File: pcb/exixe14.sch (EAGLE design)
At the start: 51 parts

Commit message: refining board design for production run
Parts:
- removed R17: 10K, joyAnalog:RESISTOR0805-RES
- renumbered U$2 to IC1
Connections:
- net +3V3: no longer R17.2
- net NRST: no longer R17.1
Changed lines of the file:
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@@
 <parts>
 <part name="N1" library="russian-nixies" deviceset="IN-14" device=""/>
-<part name="U$2" library="nixx" deviceset="STM32F042K6" device=""/>
+<part name="IC1" library="nixx" deviceset="STM32F042K6" device=""/>
 <part name="JP2" library="pinhead" deviceset="PINHD-1X7" device=""/>
 <part name="Q1" library="nixx" deviceset="BF820" device=""/>
@@
 <part name="R15" library="joyAnalog" deviceset="RESISTOR" device="0805-RES" value="680"/>
 <part name="R16" library="joyAnalog" deviceset="RESISTOR" device="0805-RES" value="330"/>
-<part name="R17" library="joyAnalog" deviceset="RESISTOR" device="0805-RES" value="10K"/>
 <part name="R18" library="joyAnalog" deviceset="RESISTOR" device="0805-RES" value="10K"/>
-<part name="+3V5" library="joyAnalog" deviceset="+3V3" device=""/>
 <part name="+3V6" library="joyAnalog" deviceset="+3V3" device=""/>
 <part name="TP1" library="testpad" deviceset="PTR1" device="TP13R" value="PTR1TP13R"/>
@@
 <instances>
 <instance part="N1" gate="G$1" x="220.98" y="-30.48"/>
-<instance part="U$2" gate="G$1" x="386.08" y="104.14"/>
+<instance part="IC1" gate="G$1" x="386.08" y="104.14"/>
 <instance part="JP2" gate="A" x="332.74" y="-40.64"/>
 <instance part="Q1" gate="A" x="101.6" y="48.26"/>
@@
 <instance part="R15" gate="G$1" x="495.3" y="7.62"/>
 <instance part="R16" gate="G$1" x="495.3" y="-7.62"/>
-<instance part="R17" gate="G$1" x="340.36" y="-27.94" rot="R90"/>
 <instance part="R18" gate="G$1" x="347.98" y="-38.1" rot="R90"/>
-<instance part="+3V5" gate="G$1" x="340.36" y="-20.32" rot="MR0"/>
 <instance part="+3V6" gate="G$1" x="347.98" y="-30.48" rot="MR0"/>
 <instance part="TP1" gate="G$1" x="381" y="55.88" rot="R270"/>
@@
 <segment>
 <pinref part="GND13" gate="1" pin="GND"/>
-<pinref part="U$2" gate="G$1" pin="VSS"/>
+<pinref part="IC1" gate="G$1" pin="VSS"/>
 <wire x1="375.92" y1="38.1" x2="383.54" y2="38.1" width="0.1524" layer="91"/>
 </segment>
@@
 <segment>
 <pinref part="+3V1" gate="G$1" pin="+3V3"/>
-<pinref part="U$2" gate="G$1" pin="VDD"/>
+<pinref part="IC1" gate="G$1" pin="VDD"/>
 <wire x1="375.92" y1="101.6" x2="383.54" y2="101.6" width="0.1524" layer="91"/>
-<pinref part="U$2" gate="G$1" pin="VDDA"/>
+<pinref part="IC1" gate="G$1" pin="VDDA"/>
 <wire x1="383.54" y1="99.06" x2="375.92" y2="99.06" width="0.1524" layer="91"/>
 <wire x1="375.92" y1="99.06" x2="375.92" y2="101.6" width="0.1524" layer="91"/>
@@
 <pinref part="D1" gate="G$1" pin="A"/>
 <wire x1="459.74" y1="0" x2="467.36" y2="0" width="0.1524" layer="91"/>
-</segment>
-<segment>
-<pinref part="R17" gate="G$1" pin="2"/>
-<pinref part="+3V5" gate="G$1" pin="+3V3"/>
 </segment>
 <segment>
@@
 </segment>
 <segment>
-<pinref part="U$2" gate="G$1" pin="PA5"/>
+<pinref part="IC1" gate="G$1" pin="PA5"/>
 <wire x1="439.42" y1="88.9" x2="424.18" y2="88.9" width="0.1524" layer="91"/>
 <label x="426.72" y="88.9" size="1.778" layer="95"/>
@@
 </segment>
 <segment>
-<pinref part="U$2" gate="G$1" pin="PA6"/>
+<pinref part="IC1" gate="G$1" pin="PA6"/>
 <wire x1="439.42" y1="86.36" x2="424.18" y2="86.36" width="0.1524" layer="91"/>
 <label x="426.72" y="86.36" size="1.778" layer="95"/>
@@
 </segment>
 <segment>
-<pinref part="U$2" gate="G$1" pin="PA7"/>
+<pinref part="IC1" gate="G$1" pin="PA7"/>
 <wire x1="439.42" y1="83.82" x2="424.18" y2="83.82" width="0.1524" layer="91"/>
 <label x="426.72" y="83.82" size="1.778" layer="95"/>
@@
 <segment>
 <label x="426.72" y="60.96" size="1.778" layer="95"/>
-<pinref part="U$2" gate="G$1" pin="PA15"/>
+<pinref part="IC1" gate="G$1" pin="PA15"/>
 <wire x1="439.42" y1="60.96" x2="424.18" y2="60.96" width="0.1524" layer="91"/>
 </segment>
@@
 </segment>
 <segment>
-<pinref part="U$2" gate="G$1" pin="PA13/SWDIO"/>
+<pinref part="IC1" gate="G$1" pin="PA13/SWDIO"/>
 <wire x1="439.42" y1="66.04" x2="424.18" y2="66.04" width="0.1524" layer="91"/>
 <label x="426.72" y="66.04" size="1.778" layer="95"/>
@@
 </segment>
 <segment>
-<pinref part="U$2" gate="G$1" pin="PA14/SWCLK"/>
+<pinref part="IC1" gate="G$1" pin="PA14/SWCLK"/>
 <wire x1="439.42" y1="63.5" x2="424.18" y2="63.5" width="0.1524" layer="91"/>
 <label x="426.72" y="63.5" size="1.778" layer="95"/>
@@
 <net name="NRST" class="0">
 <segment>
-<pinref part="U$2" gate="G$1" pin="NRST"/>
+<pinref part="IC1" gate="G$1" pin="NRST"/>
 <wire x1="370.84" y1="78.74" x2="383.54" y2="78.74" width="0.1524" layer="91"/>
 <label x="370.84" y="78.74" size="1.778" layer="95"/>
@@
 <wire x1="307.34" y1="-33.02" x2="330.2" y2="-33.02" width="0.1524" layer="91"/>
 <label x="307.34" y="-33.02" size="1.778" layer="95"/>
-<pinref part="R17" gate="G$1" pin="1"/>
-<wire x1="340.36" y1="-33.02" x2="330.2" y2="-33.02" width="0.1524" layer="91"/>
-<junction x="330.2" y="-33.02"/>
 </segment>
 </net>
 <net name="UART_TX" class="0">
 <segment>
-<pinref part="U$2" gate="G$1" pin="PB6"/>
+<pinref part="IC1" gate="G$1" pin="PB6"/>
 <wire x1="439.42" y1="43.18" x2="424.18" y2="43.18" width="0.1524" layer="91"/>
 <label x="426.72" y="43.18" size="1.778" layer="95"/>
@@
 <segment>
 <label x="426.72" y="48.26" size="1.778" layer="95"/>
-<pinref part="U$2" gate="G$1" pin="PB4"/>
+<pinref part="IC1" gate="G$1" pin="PB4"/>
 <wire x1="439.42" y1="48.26" x2="424.18" y2="48.26" width="0.1524" layer="91"/>
 </segment>
@@
 </segment>
 <segment>
-<pinref part="U$2" gate="G$1" pin="PB8"/>
+<pinref part="IC1" gate="G$1" pin="PB8"/>
 <label x="426.72" y="38.1" size="1.778" layer="95"/>
 <wire x1="439.42" y1="38.1" x2="429.26" y2="38.1" width="0.1524" layer="91"/>
@@
 </segment>
 <segment>
-<pinref part="U$2" gate="G$1" pin="PA10"/>
+<pinref part="IC1" gate="G$1" pin="PA10"/>
 <wire x1="439.42" y1="73.66" x2="424.18" y2="73.66" width="0.1524" layer="91"/>
 <label x="426.72" y="73.66" size="1.778" layer="95"/>
@@
 <segment>
 <label x="426.72" y="45.72" size="1.778" layer="95"/>
-<pinref part="U$2" gate="G$1" pin="PB5"/>
+<pinref part="IC1" gate="G$1" pin="PB5"/>
 <wire x1="439.42" y1="45.72" x2="424.18" y2="45.72" width="0.1524" layer="91"/>
 </segment>
@@
 </segment>
 <segment>
-<pinref part="U$2" gate="G$1" pin="PA8"/>
+<pinref part="IC1" gate="G$1" pin="PA8"/>
 <wire x1="439.42" y1="78.74" x2="424.18" y2="78.74" width="0.1524" layer="91"/>
 <label x="426.72" y="78.74" size="1.778" layer="95"/>
@@
 </segment>
 <segment>
-<pinref part="U$2" gate="G$1" pin="PA9"/>
+<pinref part="IC1" gate="G$1" pin="PA9"/>
 <wire x1="439.42" y1="76.2" x2="424.18" y2="76.2" width="0.1524" layer="91"/>
 <label x="426.72" y="76.2" size="1.778" layer="95"/>
@@
 </segment>
 <segment>
-<pinref part="U$2" gate="G$1" pin="PA11"/>
+<pinref part="IC1" gate="G$1" pin="PA11"/>
 <wire x1="439.42" y1="71.12" x2="424.18" y2="71.12" width="0.1524" layer="91"/>
 <label x="426.72" y="71.12" size="1.778" layer="95"/>
@@
 </segment>
 <segment>
-<pinref part="U$2" gate="G$1" pin="PA0"/>
+<pinref part="IC1" gate="G$1" pin="PA0"/>
 <wire x1="439.42" y1="101.6" x2="424.18" y2="101.6" width="0.1524" layer="91"/>
 <label x="426.72" y="101.6" size="1.778" layer="95"/>
@@
 <segment>
 <label x="426.72" y="40.64" size="1.778" layer="95"/>
-<pinref part="U$2" gate="G$1" pin="PB7"/>
+<pinref part="IC1" gate="G$1" pin="PB7"/>
 <wire x1="439.42" y1="40.64" x2="424.18" y2="40.64" width="0.1524" layer="91"/>
 </segment>
@@
 </segment>
 <segment>
-<pinref part="U$2" gate="G$1" pin="PA3"/>
+<pinref part="IC1" gate="G$1" pin="PA3"/>
 <wire x1="439.42" y1="93.98" x2="424.18" y2="93.98" width="0.1524" layer="91"/>
 <label x="426.72" y="93.98" size="1.778" layer="95"/>
@@
 </segment>
 <segment>
-<pinref part="U$2" gate="G$1" pin="PA2"/>
+<pinref part="IC1" gate="G$1" pin="PA2"/>
 <wire x1="439.42" y1="96.52" x2="424.18" y2="96.52" width="0.1524" layer="91"/>
 <label x="426.72" y="96.52" size="1.778" layer="95"/>
@@
 </segment>
 <segment>
-<pinref part="U$2" gate="G$1" pin="PA1"/>
+<pinref part="IC1" gate="G$1" pin="PA1"/>
 <wire x1="439.42" y1="99.06" x2="424.18" y2="99.06" width="0.1524" layer="91"/>
 <label x="426.72" y="99.06" size="1.778" layer="95"/>
@@
 <segment>
 <wire x1="439.42" y1="55.88" x2="424.18" y2="55.88" width="0.1524" layer="91"/>
-<pinref part="U$2" gate="G$1" pin="PB0"/>
+<pinref part="IC1" gate="G$1" pin="PB0"/>
 <label x="426.72" y="55.88" size="1.778" layer="95"/>
 </segment>
@@
 </segment>
 <segment>
-<pinref part="U$2" gate="G$1" pin="PA4"/>
+<pinref part="IC1" gate="G$1" pin="PA4"/>
 <wire x1="439.42" y1="91.44" x2="424.18" y2="91.44" width="0.1524" layer="91"/>
 <label x="426.72" y="91.44" size="1.778" layer="95"/>
@@
 </segment>
 <segment>
-<pinref part="U$2" gate="G$1" pin="PB1"/>
+<pinref part="IC1" gate="G$1" pin="PB1"/>
 <wire x1="439.42" y1="53.34" x2="424.18" y2="53.34" width="0.1524" layer="91"/>
 <label x="426.72" y="53.34" size="1.778" layer="95"/>
@@
 <net name="N$2" class="0">
 <segment>
-<pinref part="U$2" gate="G$1" pin="PF0/OSC_IN"/>
+<pinref part="IC1" gate="G$1" pin="PF0/OSC_IN"/>
 <pinref part="TP1" gate="G$1" pin="TP"/>
 </segment>
@@
 <net name="N$16" class="0">
 <segment>
-<pinref part="U$2" gate="G$1" pin="PF1/OSC_OUT"/>
+<pinref part="IC1" gate="G$1" pin="PF1/OSC_OUT"/>
 <pinref part="TP2" gate="G$1" pin="TP"/>
 </segment>
@@
 <net name="BAKE" class="0">
 <segment>
-<pinref part="U$2" gate="G$1" pin="PA12"/>
+<pinref part="IC1" gate="G$1" pin="PA12"/>
 <wire x1="439.42" y1="68.58" x2="424.18" y2="68.58" width="0.1524" layer="91"/>
 <label x="426.72" y="68.58" size="1.778" layer="95"/>
@@
 <net name="N$25" class="0">
 <segment>
-<pinref part="U$2" gate="G$1" pin="PB3"/>
+<pinref part="IC1" gate="G$1" pin="PB3"/>
 <pinref part="TP4" gate="G$1" pin="TP"/>
 <wire x1="424.18" y1="50.8" x2="449.58" y2="50.8" width="0.1524" layer="91"/>

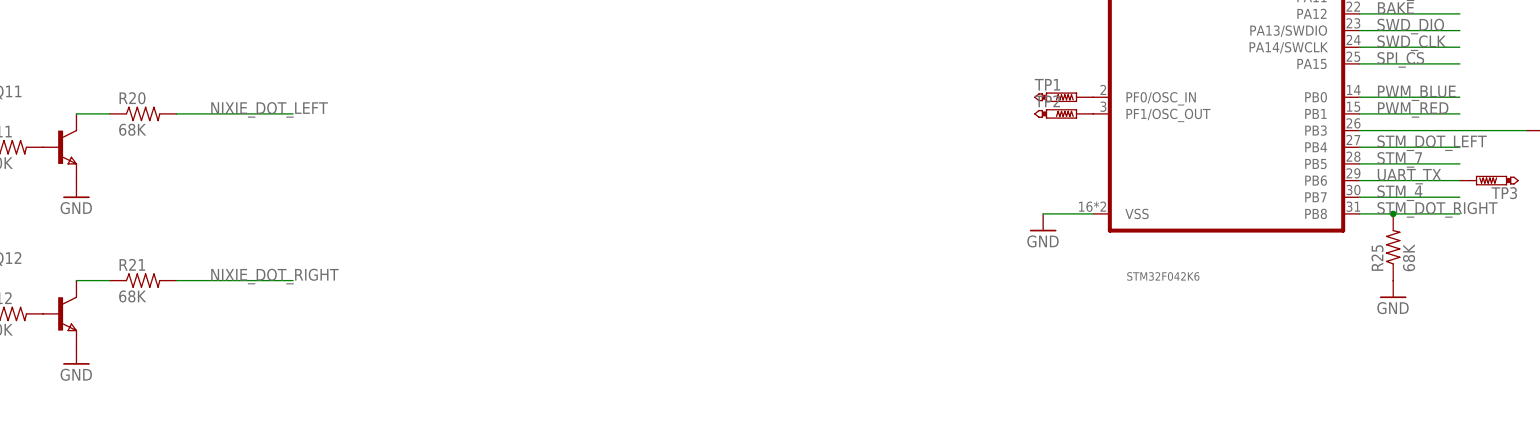
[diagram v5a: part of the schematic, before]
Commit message: adjusted passive values
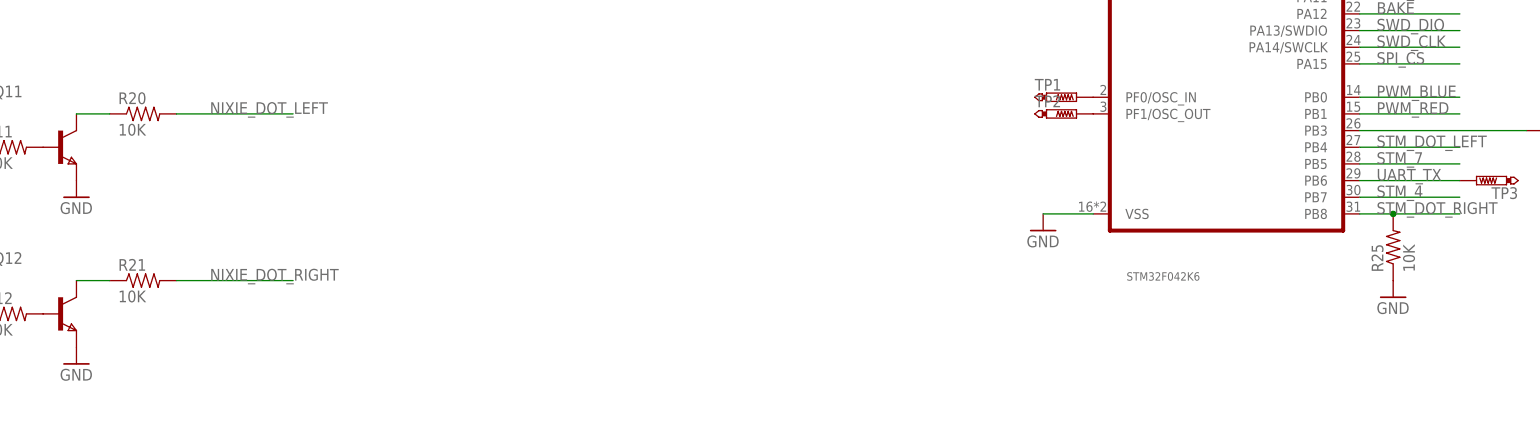
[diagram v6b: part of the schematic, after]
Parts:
- R20, R21, R25: value 68K -> 10K
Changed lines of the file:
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@@
 <part name="TP2" library="testpad" deviceset="PTR1" device="TP13R" value="PTR1TP13R"/>
 <part name="TP3" library="testpad" deviceset="PTR1" device="TP13R" value="PTR1TP13R"/>
-<part name="R20" library="joyAnalog" deviceset="RESISTOR" device="0805-RES" value="68K"/>
-<part name="R21" library="joyAnalog" deviceset="RESISTOR" device="0805-RES" value="68K"/>
-<part name="R25" library="joyAnalog" deviceset="RESISTOR" device="0805-RES" value="68K"/>
+<part name="R20" library="joyAnalog" deviceset="RESISTOR" device="0805-RES" value="10K"/>
+<part name="R21" library="joyAnalog" deviceset="RESISTOR" device="0805-RES" value="10K"/>
+<part name="R25" library="joyAnalog" deviceset="RESISTOR" device="0805-RES" value="10K"/>
 <part name="GND16" library="joyAnalog" deviceset="GND" device=""/>
 <part name="TP4" library="testpad" deviceset="PTR1" device="TP13R" value="PTR1TP13R"/>

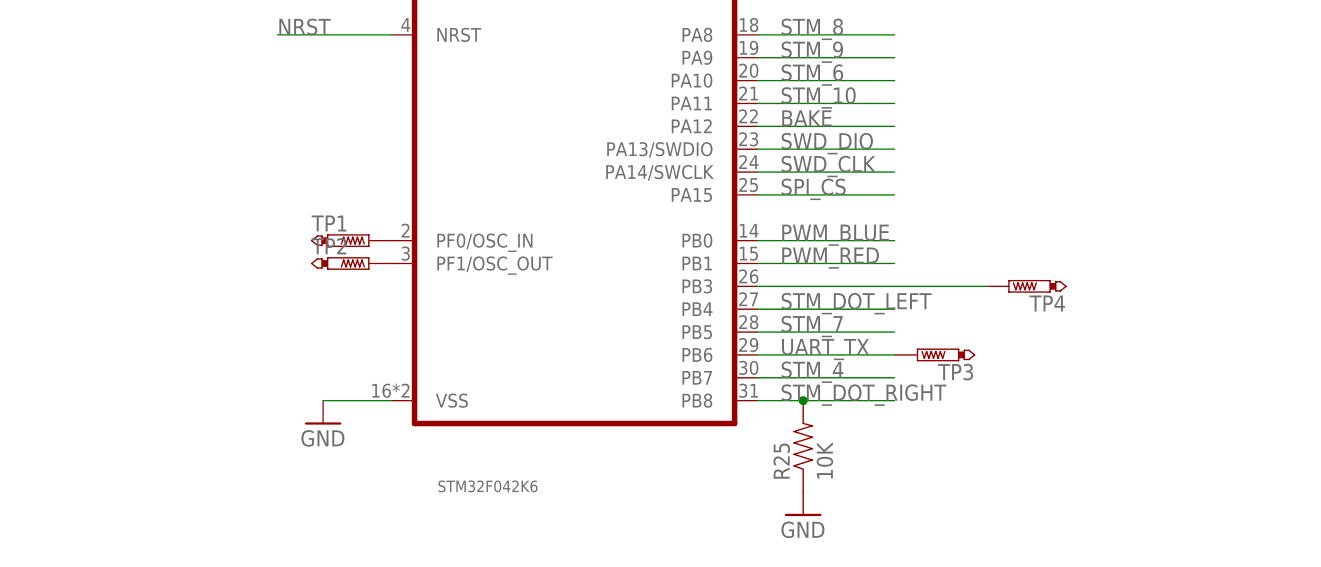
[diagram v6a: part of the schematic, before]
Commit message: changed testpoints to unpopulated resistors
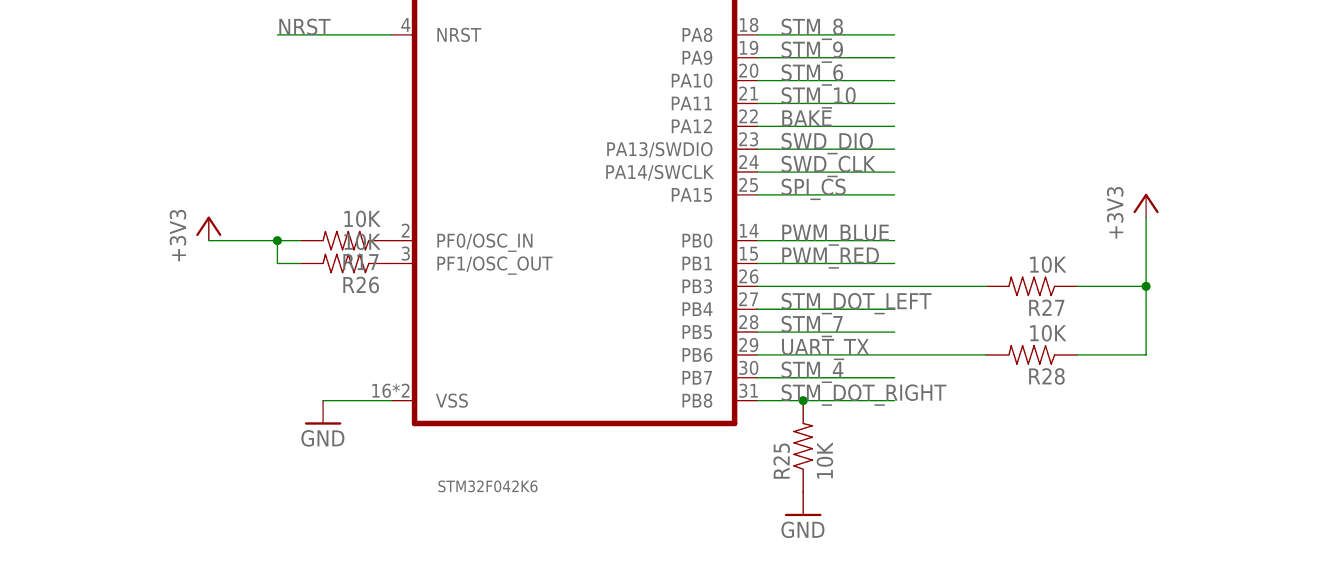
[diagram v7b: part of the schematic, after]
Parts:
- removed TP1, TP2, TP3, TP4: PTR1TP13R, testpad:PTR1TP13R
- added R17, R26, R27, R28: 10K, joyAnalog:RESISTOR0805-RES
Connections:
- net +3V3: now also R17.2, R26.2, R27.1, R28.1
- net N$16: now also R26.1; no longer TP2.TP
- net N$2: now also R17.1; no longer TP1.TP
- net N$25: now also R27.2; no longer TP4.TP
- net UART_TX: now also R28.2; no longer TP3.TP
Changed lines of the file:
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@@
 <part name="R18" library="joyAnalog" deviceset="RESISTOR" device="0805-RES" value="10K"/>
 <part name="+3V6" library="joyAnalog" deviceset="+3V3" device=""/>
-<part name="TP1" library="testpad" deviceset="PTR1" device="TP13R" value="PTR1TP13R"/>
 <part name="R22" library="joyAnalog" deviceset="RESISTOR" device="0805-RES" value="1M"/>
 <part name="R23" library="joyAnalog" deviceset="RESISTOR" device="0805-RES" value="68K"/>
@@
 <part name="GND18" library="joyAnalog" deviceset="GND" device=""/>
 <part name="R19" library="joyAnalog" deviceset="RESISTOR" device="0805-RES" value="1M"/>
-<part name="TP2" library="testpad" deviceset="PTR1" device="TP13R" value="PTR1TP13R"/>
-<part name="TP3" library="testpad" deviceset="PTR1" device="TP13R" value="PTR1TP13R"/>
 <part name="R20" library="joyAnalog" deviceset="RESISTOR" device="0805-RES" value="10K"/>
 <part name="R21" library="joyAnalog" deviceset="RESISTOR" device="0805-RES" value="10K"/>
 <part name="R25" library="joyAnalog" deviceset="RESISTOR" device="0805-RES" value="10K"/>
 <part name="GND16" library="joyAnalog" deviceset="GND" device=""/>
-<part name="TP4" library="testpad" deviceset="PTR1" device="TP13R" value="PTR1TP13R"/>
+<part name="+3V5" library="joyAnalog" deviceset="+3V3" device=""/>
+<part name="R17" library="joyAnalog" deviceset="RESISTOR" device="0805-RES" value="10K"/>
+<part name="R26" library="joyAnalog" deviceset="RESISTOR" device="0805-RES" value="10K"/>
+<part name="+3V7" library="joyAnalog" deviceset="+3V3" device=""/>
+<part name="R27" library="joyAnalog" deviceset="RESISTOR" device="0805-RES" value="10K"/>
+<part name="R28" library="joyAnalog" deviceset="RESISTOR" device="0805-RES" value="10K"/>
 </parts>
 <sheets>
@@
 <instance part="R18" gate="G$1" x="347.98" y="-38.1" rot="R90"/>
 <instance part="+3V6" gate="G$1" x="347.98" y="-30.48" rot="MR0"/>
-<instance part="TP1" gate="G$1" x="381" y="55.88" rot="R270"/>
 <instance part="R22" gate="G$1" x="391.16" y="-63.5" rot="R180"/>
 <instance part="R23" gate="G$1" x="406.4" y="-73.66" rot="R90"/>
@@
 <instance part="GND18" gate="1" x="378.46" y="-76.2"/>
 <instance part="R19" gate="G$1" x="378.46" y="-58.42" rot="R270"/>
-<instance part="TP2" gate="G$1" x="381" y="53.34" rot="R270"/>
-<instance part="TP3" gate="G$1" x="441.96" y="43.18" rot="R90"/>
 <instance part="R20" gate="G$1" x="238.76" y="53.34"/>
 <instance part="R21" gate="G$1" x="238.76" y="27.94"/>
 <instance part="R25" gate="G$1" x="429.26" y="33.02" rot="R90"/>
 <instance part="GND16" gate="1" x="429.26" y="25.4"/>
-<instance part="TP4" gate="G$1" x="452.12" y="50.8" rot="R90"/>
+<instance part="+3V5" gate="G$1" x="363.22" y="58.42"/>
+<instance part="R17" gate="G$1" x="378.46" y="55.88" rot="R180"/>
+<instance part="R26" gate="G$1" x="378.46" y="53.34" rot="R180"/>
+<instance part="+3V7" gate="G$1" x="467.36" y="60.96"/>
+<instance part="R27" gate="G$1" x="454.66" y="50.8" rot="R180"/>
+<instance part="R28" gate="G$1" x="454.66" y="43.18" rot="R180"/>
 </instances>
 <busses>
@@
 <wire x1="424.18" y1="-45.72" x2="431.8" y2="-45.72" width="0.1524" layer="91"/>
 </segment>
+<segment>
+<pinref part="+3V5" gate="G$1" pin="+3V3"/>
+<pinref part="R17" gate="G$1" pin="2"/>
+<wire x1="363.22" y1="55.88" x2="370.84" y2="55.88" width="0.1524" layer="91"/>
+<pinref part="R26" gate="G$1" pin="2"/>
+<wire x1="370.84" y1="55.88" x2="373.38" y2="55.88" width="0.1524" layer="91"/>
+<wire x1="373.38" y1="53.34" x2="370.84" y2="53.34" width="0.1524" layer="91"/>
+<wire x1="370.84" y1="53.34" x2="370.84" y2="55.88" width="0.1524" layer="91"/>
+<junction x="370.84" y="55.88"/>
+</segment>
+<segment>
+<pinref part="R28" gate="G$1" pin="1"/>
+<pinref part="+3V7" gate="G$1" pin="+3V3"/>
+<wire x1="459.74" y1="43.18" x2="467.36" y2="43.18" width="0.1524" layer="91"/>
+<wire x1="467.36" y1="43.18" x2="467.36" y2="50.8" width="0.1524" layer="91"/>
+<pinref part="R27" gate="G$1" pin="1"/>
+<wire x1="467.36" y1="50.8" x2="467.36" y2="58.42" width="0.1524" layer="91"/>
+<wire x1="459.74" y1="50.8" x2="467.36" y2="50.8" width="0.1524" layer="91"/>
+<junction x="467.36" y="50.8"/>
+</segment>
 </net>
 <net name="SPI_SCK" class="0">
@@
 <segment>
 <pinref part="IC1" gate="G$1" pin="PB6"/>
-<wire x1="439.42" y1="43.18" x2="424.18" y2="43.18" width="0.1524" layer="91"/>
+<wire x1="449.58" y1="43.18" x2="424.18" y2="43.18" width="0.1524" layer="91"/>
 <label x="426.72" y="43.18" size="1.778" layer="95"/>
-<pinref part="TP3" gate="G$1" pin="TP"/>
+<pinref part="R28" gate="G$1" pin="2"/>
 </segment>
 </net>
@@
 </segment>
 </net>
-<net name="N$2" class="0">
-<segment>
-<pinref part="IC1" gate="G$1" pin="PF0/OSC_IN"/>
-<pinref part="TP1" gate="G$1" pin="TP"/>
-</segment>
-</net>
-<net name="N$16" class="0">
-<segment>
-<pinref part="IC1" gate="G$1" pin="PF1/OSC_OUT"/>
-<pinref part="TP2" gate="G$1" pin="TP"/>
-</segment>
-</net>
 <net name="BAKE" class="0">
 <segment>
@@
 <segment>
 <pinref part="IC1" gate="G$1" pin="PB3"/>
-<pinref part="TP4" gate="G$1" pin="TP"/>
 <wire x1="424.18" y1="50.8" x2="449.58" y2="50.8" width="0.1524" layer="91"/>
-</segment>
-</net>
+<pinref part="R27" gate="G$1" pin="2"/>
+</segment>
+</net>
+<net name="N$2" class="0">
+<segment>
+<pinref part="IC1" gate="G$1" pin="PF0/OSC_IN"/>
+<pinref part="R17" gate="G$1" pin="1"/>
+</segment>
+</net>
+<net name="N$16" class="0">
+<segment>
+<pinref part="IC1" gate="G$1" pin="PF1/OSC_OUT"/>
+<pinref part="R26" gate="G$1" pin="1"/>
+</segment>
+</net>
